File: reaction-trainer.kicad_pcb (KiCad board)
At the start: 2 copper layers, 7.5 x 2 mm, 56 parts, among them J1 TC2050, J2 Conn_01x02, J3 Conn_01x02, J4 Conn_01x02, J5 JST_PH_B2B, J6 47590-0001, U1 CH32V208WBU6, U2 MCP73831-2-OT, U3 AP1117-33, U4 C5944, U5 LIS3DH, U6 USBLC6-2SC6, Y1 32MHz, Y2 32768Hz

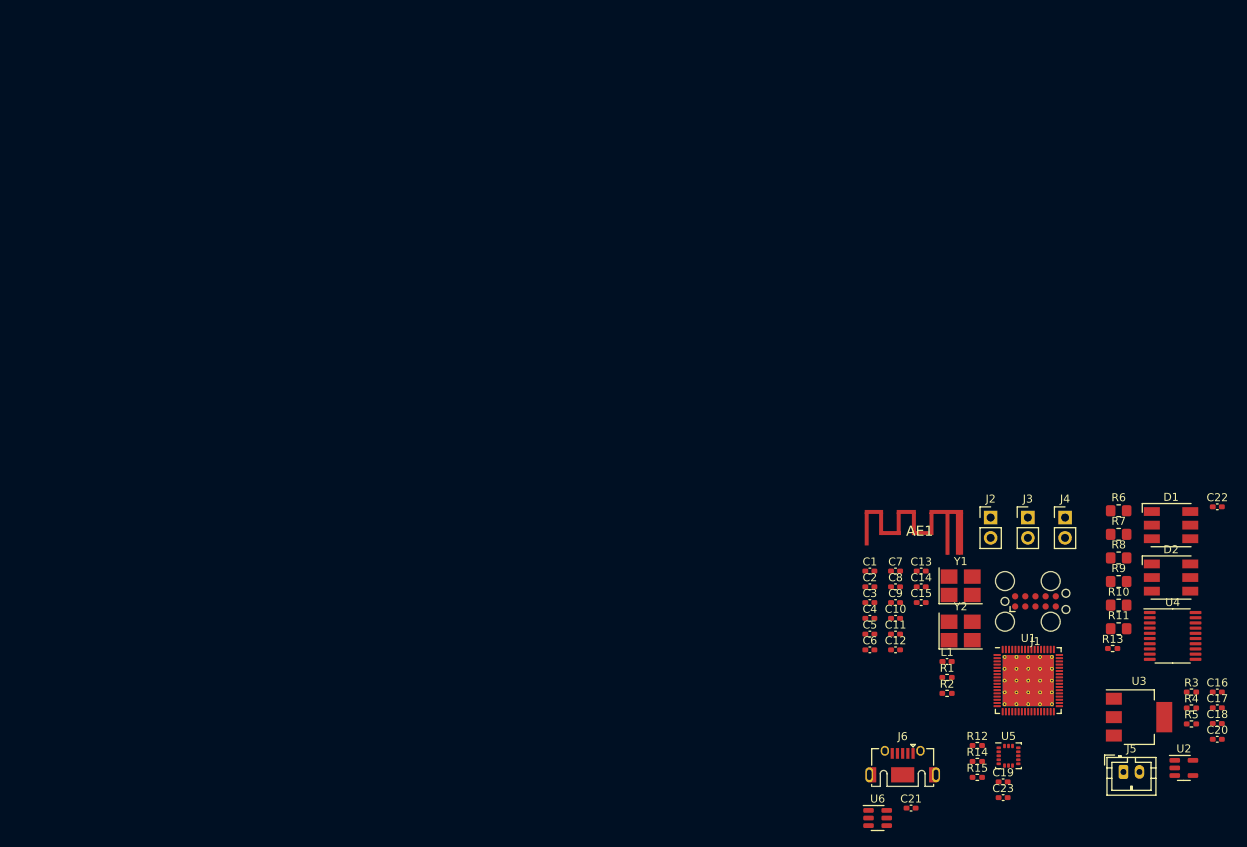
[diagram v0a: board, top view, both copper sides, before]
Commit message: Added Antenna design
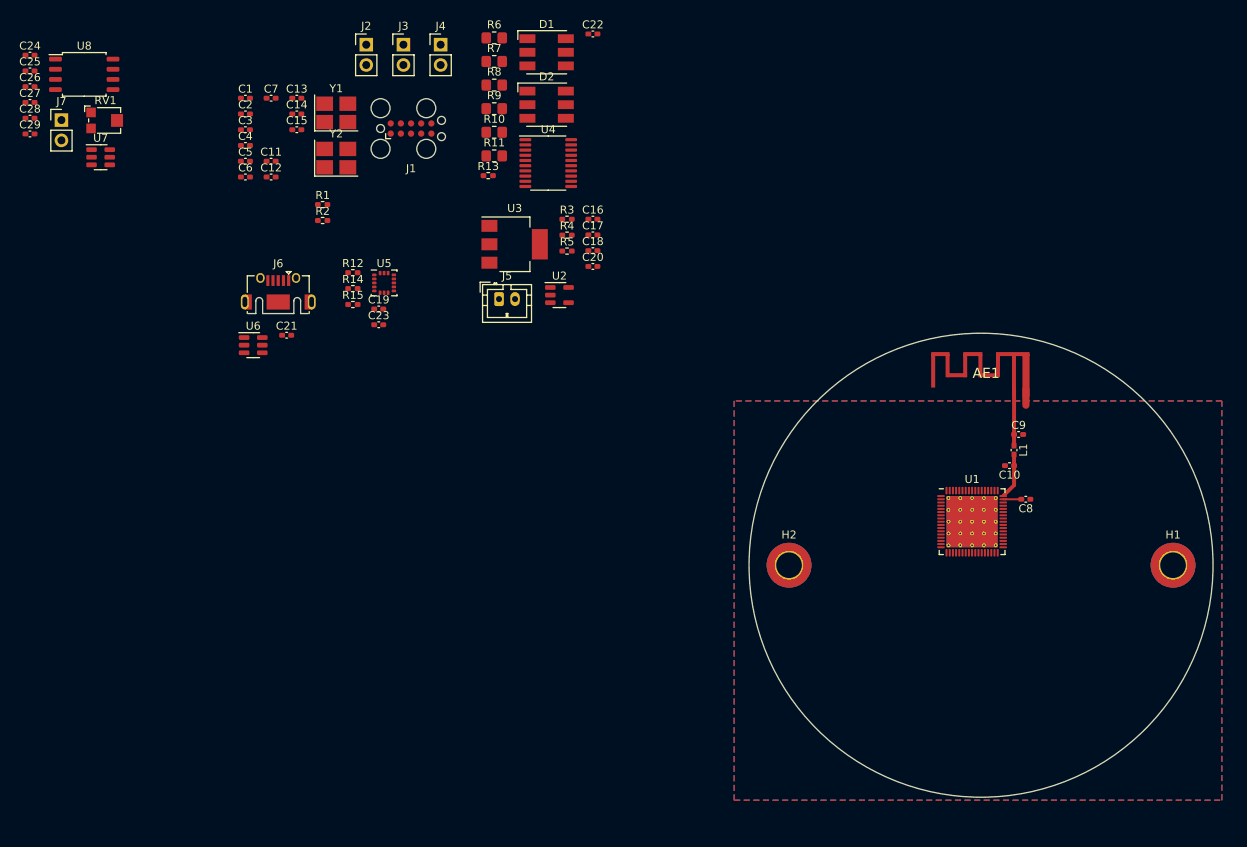
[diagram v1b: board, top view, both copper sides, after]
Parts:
- added C24: 0.1uF, Capacitor_SMD:C_0402_1005Metric_Pad0.74x0.62mm_HandSolder, F.Cu at (16.1, 26.2)
- added C25: 10uF, Capacitor_SMD:C_0402_1005Metric_Pad0.74x0.62mm_HandSolder, F.Cu at (16.1, 28.2)
- added C26: 1uF, Capacitor_SMD:C_0402_1005Metric_Pad0.74x0.62mm_HandSolder, F.Cu at (16.1, 30.2)
- added C27: 0.1uF, Capacitor_SMD:C_0402_1005Metric_Pad0.74x0.62mm_HandSolder, F.Cu at (16.1, 32.2)
- added C28: 1uF, Capacitor_SMD:C_0402_1005Metric_Pad0.74x0.62mm_HandSolder, F.Cu at (16.1, 34.1)
- added C29: 10uF, Capacitor_SMD:C_0402_1005Metric_Pad0.74x0.62mm_HandSolder, F.Cu at (16.1, 36.1)
- added H1: MountingHole_Pad, MountingHole:MountingHole_3.2mm_M3_DIN965_Pad_TopBottom, F.Cu at (159.0, 90.0)
- added H2: MountingHole_Pad, MountingHole:MountingHole_3.2mm_M3_DIN965_Pad_TopBottom, F.Cu at (111.0, 90.0)
- added J7: Speaker, Connector_PinHeader_2.54mm:PinHeader_1x02_P2.54mm_Vertical, F.Cu at (20.1, 34.4)
- added RV1: 10K, Potentiometer_SMD:Potentiometer_Bourns_TC33X_Vertical, F.Cu at (25.6, 34.4)
- added U7: PAM8301, Package_TO_SOT_SMD:SOT-23-6, F.Cu at (24.9, 39.0)
- added U8: W25Q128JVS, Package_SO:SOIC-8_5.23x5.23mm_P1.27mm, F.Cu at (22.9, 28.6)
- AE1: value Antenna -> Antenna_Shield
- moved C1 97.9 mm to (43.0, 31.6)
- moved C11 97.9 mm to (46.3, 39.5)
- moved C12 97.9 mm to (46.3, 41.5)
- moved C18 97.9 mm to (86.5, 50.7)
- moved C2 97.9 mm to (43.0, 33.6)
- moved C3 97.9 mm to (43.0, 35.6)
- moved C4 97.9 mm to (43.0, 37.5)
- moved C5 97.9 mm to (43.0, 39.5)
- moved C6 97.9 mm to (43.0, 41.5)
- moved C7 97.9 mm to (46.3, 31.6)
- moved D2 97.9 mm to (80.7, 32.4)
- moved J1 97.9 mm to (63.8, 35.4)
- moved J5 97.9 mm to (74.8, 56.7)
- moved J6 97.9 mm to (47.1, 57.1)
- moved R12 97.9 mm to (56.5, 53.4)
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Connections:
- net Net-(AE1-A) renamed /CH32V208W/ANT
- net Net-(U1-ANT) renamed /CH32V208W/ANT1
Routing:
- net /CH32V208W/ANT1: track 0.00 -> 9.49 mm
- net /CH32V208W/ANT: track 0.00 -> 7.04 mm
- net Net-(U1-VINTA): track 0.00 -> 2.26 mm
- net GND: track 0.00 -> 2.00 mm
- added copper zone on B.Cu, net GND
- added copper zone on F.Cu, net GND
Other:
- board size 7.5 x 2 mm -> 58 x 58 mm

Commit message: Removed audio, more routing
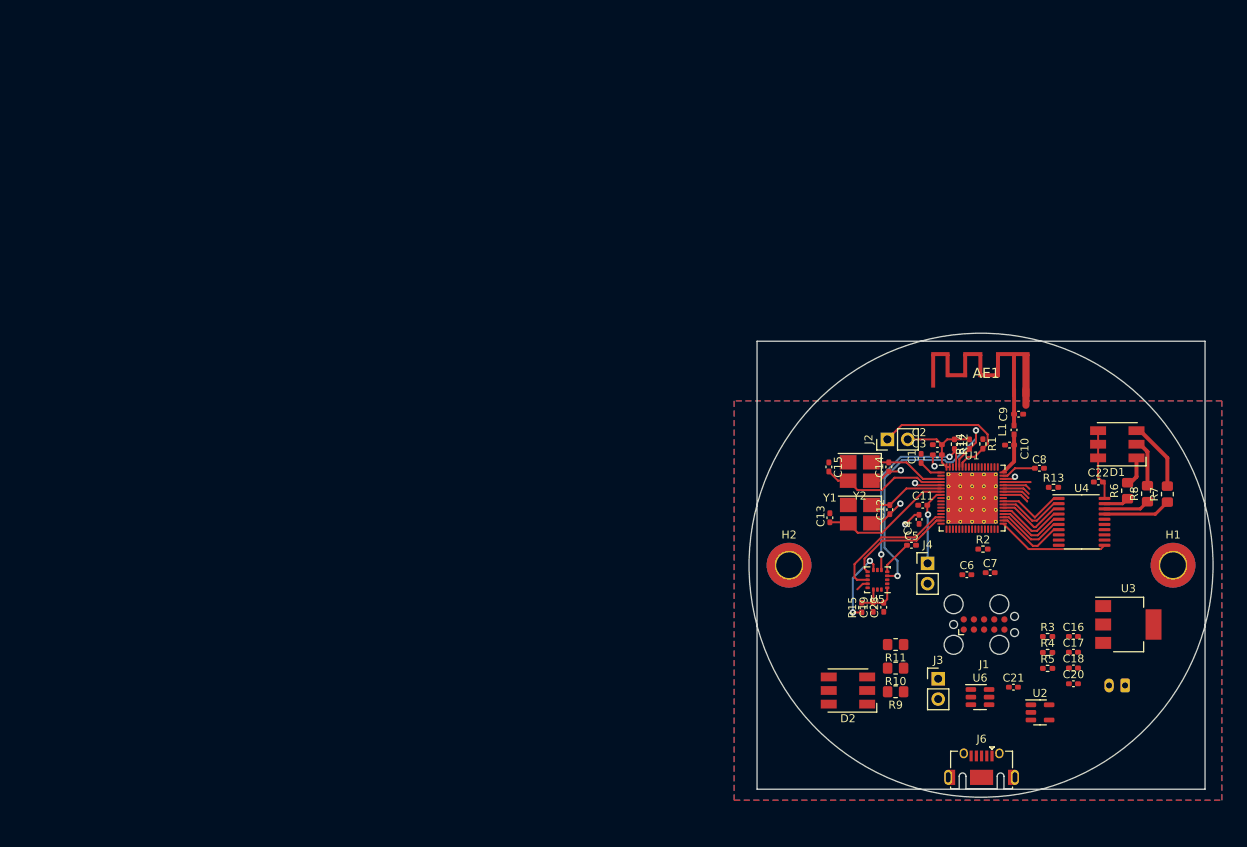
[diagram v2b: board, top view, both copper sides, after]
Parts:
- removed C24, C27: 0.1uF, Capacitor_SMD:C_0402_1005Metric_Pad0.74x0.62mm_HandSolder
- removed C25, C29: 10uF, Capacitor_SMD:C_0402_1005Metric_Pad0.74x0.62mm_HandSolder
- removed C26, C28: 1uF, Capacitor_SMD:C_0402_1005Metric_Pad0.74x0.62mm_HandSolder
- removed J7: Speaker, Connector_PinHeader_2.54mm:PinHeader_1x02_P2.54mm_Vertical
- removed RV1: 10K, Potentiometer_SMD:Potentiometer_Bourns_TC33X_Vertical
- removed U7: PAM8301, Package_TO_SOT_SMD:SOT-23-6
- removed U8: W25Q128JVS, Package_SO:SOIC-8_5.23x5.23mm_P1.27mm
- J5: moved to B.Cu
- moved C7 107.7 mm to (136.1, 90.9)
- moved J6 106.1 mm to (135.1, 116.5)
- moved J3 103.7 mm to (129.6, 104.2)
- moved C6 103.0 mm to (133.2, 91.2)
- moved C21 100.9 mm to (139.0, 105.2)
- moved U6 100.9 mm to (134.9, 106.5)
- moved R7 100.0 mm to (158.3, 81.1), turned to 90 degrees
- moved R6 97.3 mm to (153.3, 80.7), turned to 90 degrees
- moved R8 96.3 mm to (155.8, 81.1), turned to 90 degrees
- moved C4 96.3 mm to (127.3, 84.3), turned to 90 degrees
- moved C5 96.1 mm to (126.3, 87.5)
- moved C2 95.9 mm to (129.5, 74.9), turned to 180 degrees
- moved C1 95.7 mm to (127.5, 76.6), turned to -90 degrees
- moved C3 95.6 mm to (129.5, 76.2), turned to 180 degrees
- moved J1 94.7 mm to (135.4, 97.4)
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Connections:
- R12 pad 2: /Motion/MOTION_SDA -> /CH32V208W/SDA
- R13 pad 2: /LED/LED_ENABLE -> /CH32V208W/LED_EN
- R14 pad 1: /Motion/MOTION_SCL -> /CH32V208W/SCL
- R4 pad 1: /Power/VSENSE -> /CH32V208W/VSENSE
- R5 pad 2: /Power/VSENSE -> /CH32V208W/VSENSE
- U1 pad 15: unconnected-(U1-PA1/ADC1-Pad15) -> /CH32V208W/MOTION_INT1
- U1 pad 16: unconnected-(U1-PA2/ADC2-Pad16) -> /CH32V208W/MOTION_INT2
- U1 pad 27: unconnected-(U1-PB1/ADC9-Pad27) -> /CH32V208W/VSENSE
- U1 pad 34: unconnected-(U1-PD6-Pad34) -> /CH32V208W/STAT
- U1 pad 35: unconnected-(U1-PB12-Pad35) -> /CH32V208W/LED_LATCH
- U1 pad 36: unconnected-(U1-PB13-Pad36) -> /CH32V208W/LED_5
- U1 pad 37: unconnected-(U1-PB14-Pad37) -> /CH32V208W/LED_4
- U1 pad 38: unconnected-(U1-PB15-Pad38) -> /CH32V208W/LED_3
- U1 pad 39: unconnected-(U1-PC6/RXP-Pad39) -> /CH32V208W/LED_2
- U1 pad 40: unconnected-(U1-PC7/RXN-Pad40) -> /CH32V208W/LED_1
- U1 pad 41: unconnected-(U1-PC8/TXP-Pad41) -> /CH32V208W/LED_0
- U1 pad 42: unconnected-(U1-PC9/TXN-Pad42) -> /CH32V208W/LED_EN
- U1 pad 64: unconnected-(U1-PB8-Pad64) -> /CH32V208W/SCL
- U1 pad 65: unconnected-(U1-PB9-Pad65) -> /CH32V208W/SDA
- U2 pad 1: /Power/STAT -> /CH32V208W/STAT
- U4 pad 1: /LED/LED_ENABLE -> /CH32V208W/LED_EN
- U4 pad 11: /LED/LED_LATCH -> /CH32V208W/LED_LATCH
- U4 pad 2: /LED/LED_0 -> /CH32V208W/LED_0
- U4 pad 3: /LED/LED_1 -> /CH32V208W/LED_1
- U4 pad 4: /LED/LED_2 -> /CH32V208W/LED_2
- U4 pad 5: /LED/LED_3 -> /CH32V208W/LED_3
- U4 pad 6: /LED/LED_4 -> /CH32V208W/LED_4
- U4 pad 7: /LED/LED_5 -> /CH32V208W/LED_5
- U5 pad 11: /Motion/MOTION_INT1 -> /CH32V208W/MOTION_INT1
- U5 pad 4: /Motion/MOTION_SCL -> /CH32V208W/SCL
- U5 pad 6: /Motion/MOTION_SDA -> /CH32V208W/SDA
- U5 pad 9: /Motion/MOTION_INT2 -> /CH32V208W/MOTION_INT2
- U6 pad 4: /USB/USB_DP -> /CH32V208W/USBDP
- U6 pad 6: /USB/USB_DN -> /CH32V208W/USBDM
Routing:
- net /CH32V208W/SCL: track 0.00 -> 34.4 mm, vias 0 -> 2
- net /CH32V208W/SDA: track 0.00 -> 24.8 mm, vias 0 -> 2
- net GND: track 2.00 -> 25.4 mm, vias 0 -> 6
- net /CH32V208W/BOOT0: track 0.00 -> 19.6 mm
- net +3V3: track 0.00 -> 18.2 mm
- net /CH32V208W/MOTION_INT1: track 0.00 -> 16.6 mm
- net /CH32V208W/OSC_OUT: track 0.00 -> 16.6 mm
- net /CH32V208W/OSC32_OUT: track 0.00 -> 15.9 mm
- net /CH32V208W/LED_LATCH: track 0.00 -> 14.2 mm
- net /CH32V208W/MOTION_INT2: track 0.00 -> 13.3 mm
- net Net-(U5-CS): track 0.00 -> 9.78 mm, vias 0 -> 2
- net /CH32V208W/NRST: track 0.00 -> 9.64 mm, vias 0 -> 1
- net /CH32V208W/OSC32_IN: track 0.00 -> 9.56 mm
- net /CH32V208W/OSC_IN: track 0.00 -> 9.55 mm
- net /CH32V208W/LED_5: track 0.00 -> 9.10 mm
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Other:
- outline, holes or cut-outs redrawn

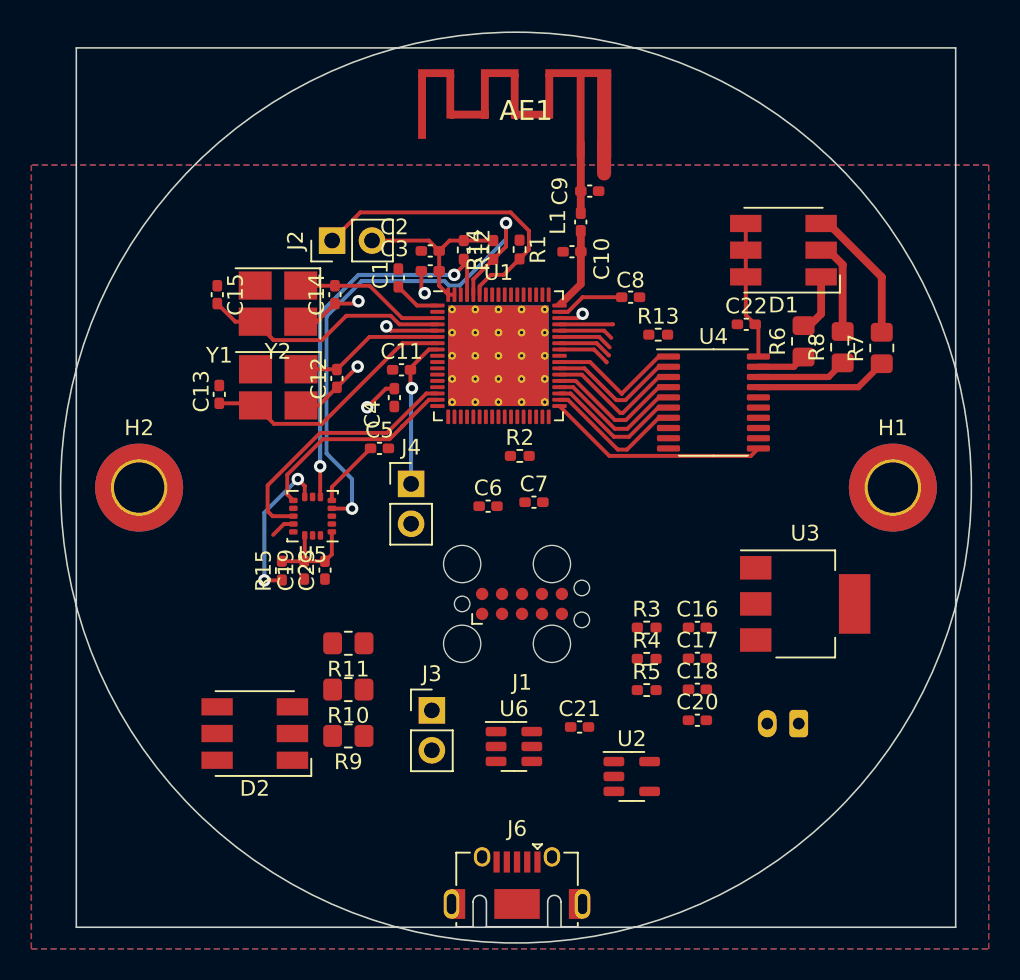
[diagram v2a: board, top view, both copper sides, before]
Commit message: Added JLPCB DRCs, antenna hatching
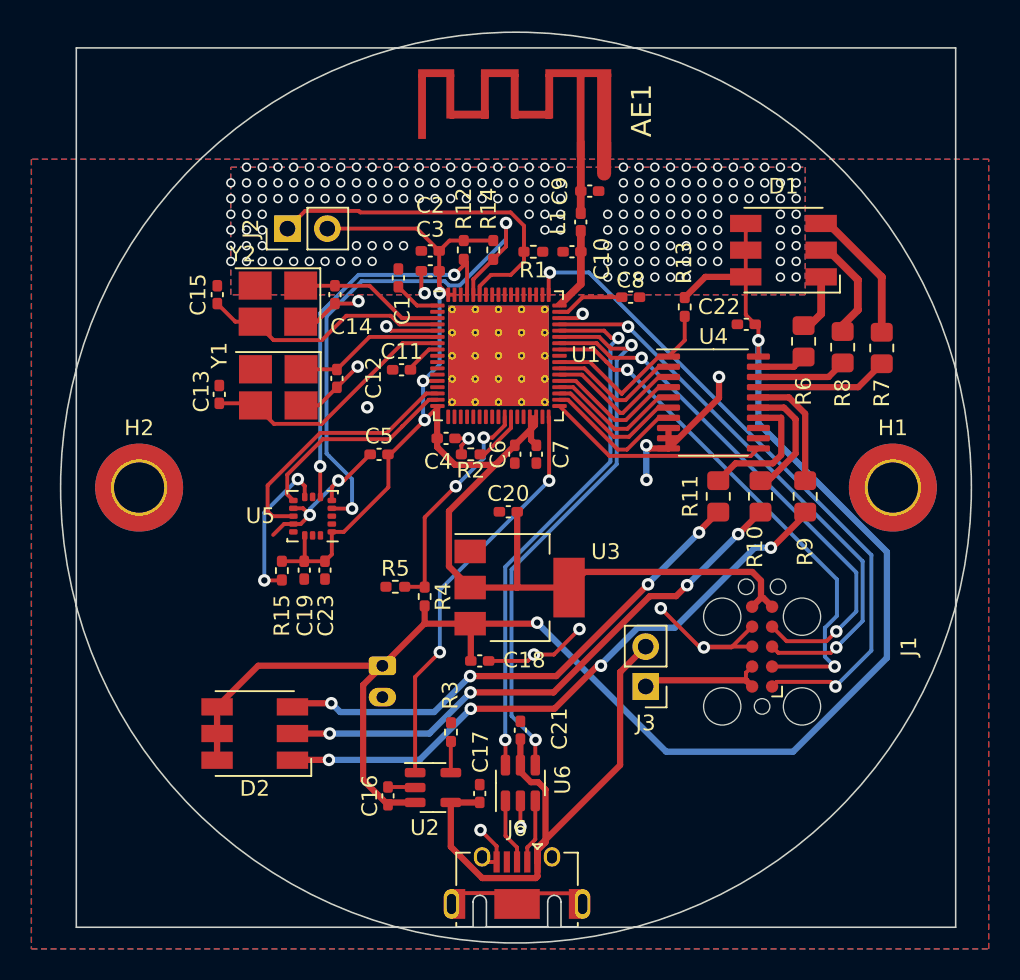
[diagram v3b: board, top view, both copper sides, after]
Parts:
- removed J4: Conn_01x02, Connector_PinHeader_2.54mm:PinHeader_1x02_P2.54mm_Vertical
- moved R9 32.9 mm to (153.4, 90.6), turned to -90 degrees
- moved R10 29.0 mm to (150.6, 90.6), turned to -90 degrees
- moved J5 26.8 mm to (126.5, 101.3), turned to -90 degrees
- moved R11 25.3 mm to (147.9, 90.6), turned to -90 degrees
- moved C16 22.4 mm to (126.8, 109.6), turned to 90 degrees
- moved U3 18.2 mm to (135.2, 96.4)
- moved C20 17.9 mm to (134.5, 91.5)
- moved R5 17.3 mm to (127.3, 96.3)
- moved C17 16.3 mm to (132.7, 109.5), turned to 90 degrees
- moved J1 15.5 mm to (150.7, 100.1), turned to 90 degrees
- moved R4 14.7 mm to (129.2, 96.9), turned to -90 degrees
- moved R3 14.1 mm to (130.9, 105.6), turned to -90 degrees
- moved C18 14.0 mm to (132.7, 101.0), turned to 180 degrees
- moved J3 13.7 mm to (143.3, 102.7), turned to 180 degrees
- moved U2 12.7 mm to (129.7, 109.1)
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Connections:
- R13 pad 1: +3V3 -> +BATT
- U6 pad 1: /USB/DN_IN -> /USB/DP_IN
- U6 pad 3: /USB/DP_IN -> /USB/DN_IN
- U6 pad 4: /CH32V208W/USBDP -> /CH32V208W/USBDM
- U6 pad 6: /CH32V208W/USBDM -> /CH32V208W/USBDP
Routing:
- net +BATT: track 8.81 -> 106.3 mm, vias 0 -> 2
- net +3V3: track 18.2 -> 92.6 mm, vias 0 -> 3
- net GND: track 25.4 -> 75.0 mm, vias 6 -> 195
- net /CH32V208W/SWCK: track 0.00 -> 43.0 mm, vias 0 -> 2
- net Net-(D2-RK): track 0.00 -> 39.5 mm, vias 0 -> 4
- net +5V: track 0.00 -> 38.0 mm
- net Net-(D2-GK): track 0.00 -> 35.6 mm, vias 0 -> 4
- net Net-(D2-BK): track 0.00 -> 32.9 mm, vias 0 -> 4
- net /CH32V208W/SWIO: track 3.40 -> 36.1 mm, vias 0 -> 2
- net /CH32V208W/USBDM: track 3.48 -> 35.5 mm, vias 0 -> 2
- net /CH32V208W/USBDP: track 3.49 -> 34.1 mm, vias 0 -> 2
- net /CH32V208W/RXD: track 3.47 -> 34.0 mm, vias 0 -> 2
- net /CH32V208W/TXD: track 3.36 -> 33.8 mm, vias 0 -> 2
- net /CH32V208W/STAT: track 0.00 -> 26.2 mm, vias 0 -> 2
- net /CH32V208W/VSENSE: track 0.00 -> 14.6 mm, vias 0 -> 2
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
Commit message: Field updates, generating fab files
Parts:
- C1, C11, C2, C21, C22, C23, C3, C4, C5, C6, C7: value 0.1uF -> 0.1uF 20%
- C10: value 1pF -> 1pF 5%
- C12, C13: value 12pF -> 12pF 5%
- C14, C15: value 12pF -> 15pF 5%
- C16, C17, C18, C19, C20: value 10uF -> 10uF 20%
- C8: value 1uF -> 10uF 20%
- C9: value 1.5pF -> 1.5pF 5%
- J2, J3: value Conn_01x02 -> DNP
- R1, R12, R13, R14, R15, R2, R3: value 10K -> 10K 5%
- R10, R8: value 30 -> 30 5% 125mW
- R11, R6, R7, R9: value 15 -> 15 5% 125mW
- R4: value 500K -> 510K 1%
- R5: value 1M -> 1M 1%
- U3: value AP1117-33 -> HT7533-1; footprint Package_TO_SOT_SMD:SOT-223-3_TabPin2 -> Package_TO_SOT_SMD:SOT-89-3
- U4: value C5944 -> 74HC573PW,118
- U5: value LIS3DH -> LIS3DHTR
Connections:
- U3 pad 2: +3V3 -> +BATT
- U3 pad 3: +BATT -> +3V3
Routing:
- net +3V3: track 92.6 -> 87.2 mm
- net GND: track 75.0 -> 78.1 mm, vias 195 -> 196
- net +BATT: track 106.3 -> 109.4 mm
